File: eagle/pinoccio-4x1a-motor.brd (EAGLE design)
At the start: 25.4 x 43.2 mm, 11 parts, among them IC1 74LVC1G04DBV, J1 POWER_JACKPTH, U1 TB6621FNG, U2 TB6621FNG

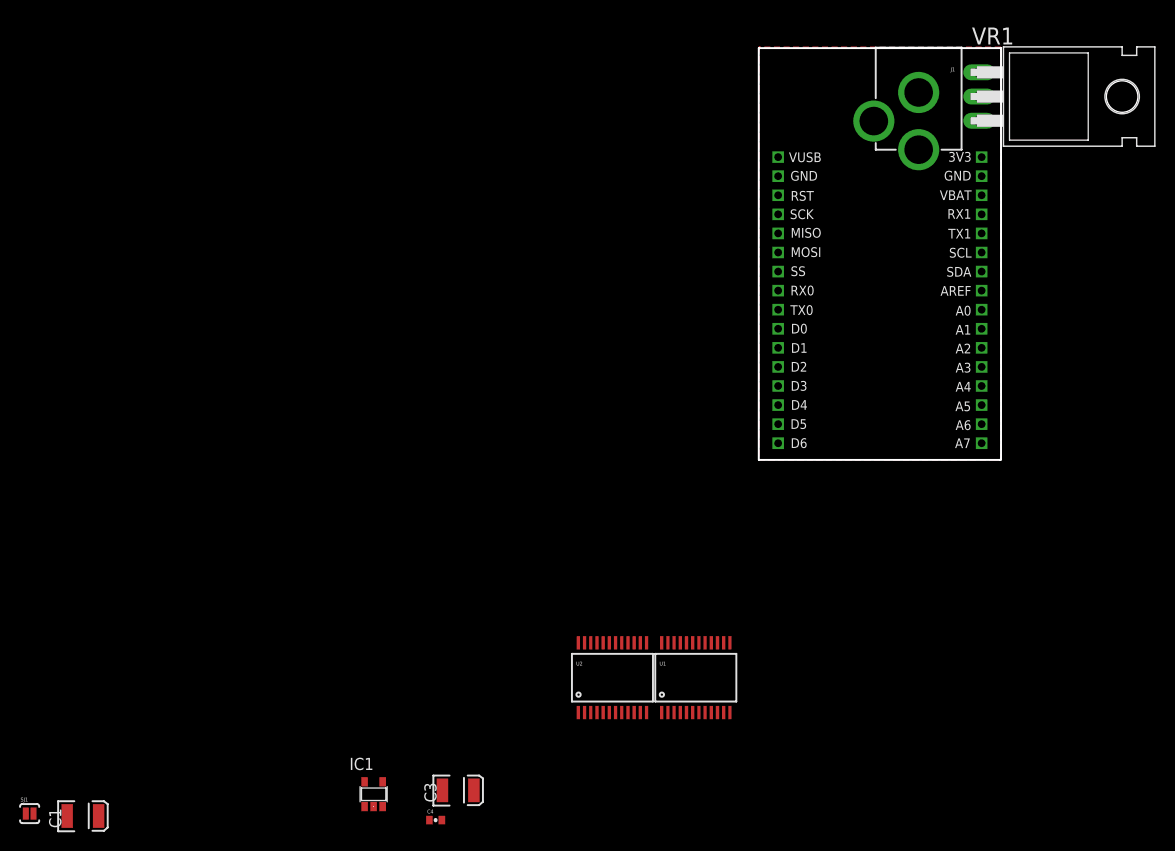
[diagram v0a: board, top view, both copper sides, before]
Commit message: Finish first draft of schematic
Initial placement.
Add design rules file from OSHPark.com
Export PDFs of schematic and board.
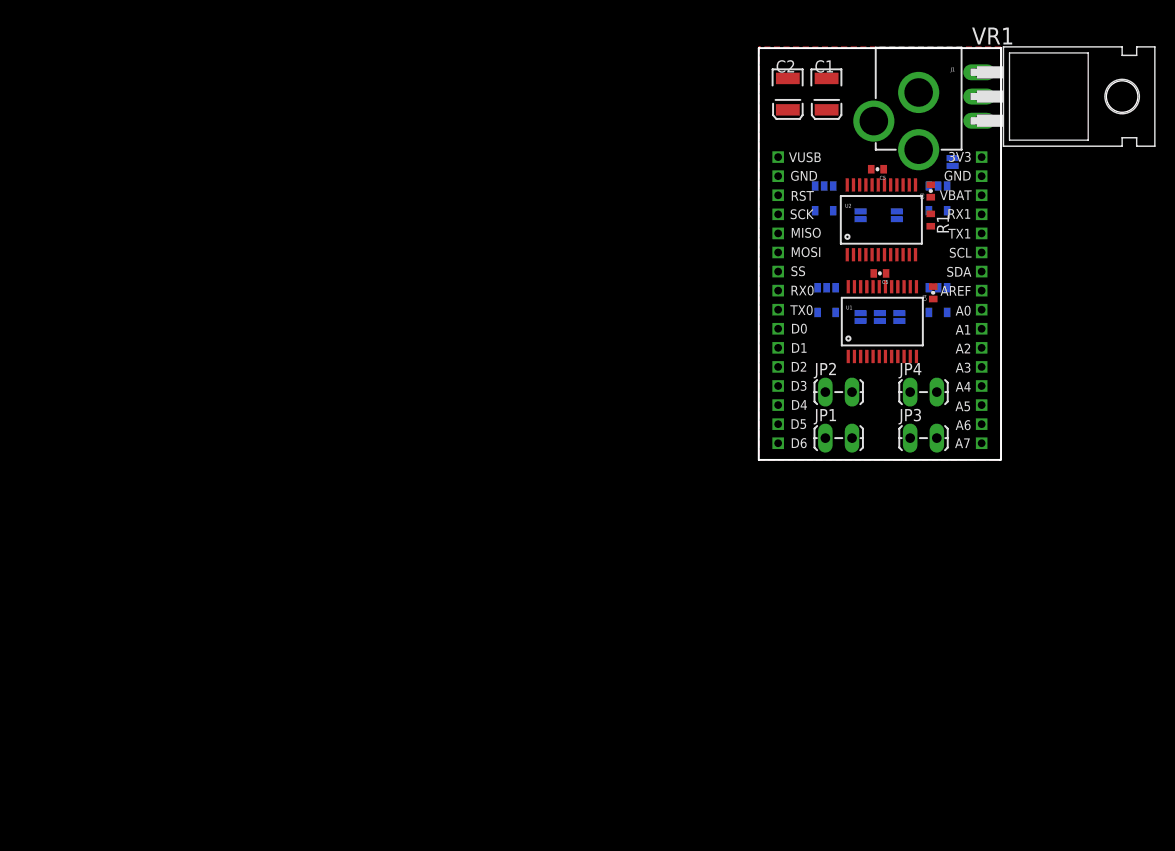
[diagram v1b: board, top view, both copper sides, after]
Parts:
- added C2: 10uf , 20V, SparkFun:EIA3528
- added C5, C6: 0.1uF, SparkFun:0402-CAP
- added IC2, IC3, IC4: 74LVC1G04DBV, 74xx-little-de:SOT23-5
- added JP1, JP2, JP3, JP4: (no value), SparkFun-Connectors:1X02_LOCK_LONGPADS
- added R1: 10k, rcl:R0402
- added SJ2, SJ3, SJ4, SJ5, SJ6: SOLDERJUMPERNC2, SparkFun-Passives:SJ_2S-NOTRACE
- C3: value 10uf , 20V -> 0.1uF; device SparkFun:EIA3528 -> SparkFun:0402-CAP
- moved C1 108.7 mm to (7.11, 46.0), turned to 270 degrees
- moved SJ1 101.5 mm to (10.7, 22.6), flipped to the bottom, turned to 270 degrees
- moved C3 80.0 mm to (18.0, 35.8), turned to 90 degrees
- moved C4 76.0 mm to (18.3, 25.1), turned to 90 degrees
- moved IC1 70.3 mm to (7.11, 24.4), flipped to the bottom, turned to 180 degrees
- moved U2 55.7 mm to (12.9, 32.8)
- moved U1 42.2 mm to (13.0, 22.1)
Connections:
- net N$3 renamed 1A2
- removed net N$1: C1.A, C3.A, C4.2, VR1.3
- removed net N$2: IC1.2, U1.21
- removed net N$4: SJ1.2
- removed net VCC: IC1.5
- new net 1B2: IC2.4, SJ2.1, U1.16
- new net 2A2: IC3.4, SJ3.1, U2.22
- new net 2B2: IC4.4, SJ4.1, U2.16
- new net M1+: JP1.2, U1.1, U1.2
- new net M1-: JP1.1, U1.5, U1.6
- new net M2+: JP2.2, U1.7, U1.8
- new net M2-: JP2.1, U1.11, U1.12
- new net M3+: JP3.2, U2.1, U2.2
- new net M3-: JP3.1, U2.5, U2.6
- new net M4+: JP4.2, U2.7, U2.8
- new net N$8: JP4.1, U2.11, U2.12
- new net STBY: R1.2, SJ5.1, U1.19, U2.19
- new net V+: C1.A, C2.A, C3.2, C4.2, J1.PWR, SJ6.1, U1.13, U1.14, U1.24, U2.13, U2.14, U2.24, VR1.3
- net A2: now also SJ4.2
- net A3: now also SJ3.2
- net A4: now also SJ2.2
- net A5: now also SJ1.2
- net A6: now also IC4.2, U2.17
- net A7: now also SJ5.2
- net D0: now also U1.23
- net D1: now also U1.15
- net D2: now also U2.23
- net D3: now also U2.15
- net D4: now also IC1.2, U1.21
- net D5: now also IC2.2, U1.17
- net D6: now also IC3.2, U2.21
- net GND: now also C2.C, C3.1, C5.1, C6.1, IC2.3, IC3.3, IC4.3, J1.GND, J1.GNDBREAK, U1.10, U1.18, U1.3, U1.4, U1.9, U2.10, U2.18, U2.3, U2.4, U2.9; no longer C3.C
- net VBAT-AE: now also SJ6.2
- net VCC-AE: now also C5.2, C6.2, IC1.5, IC2.5, IC3.5, IC4.5, R1.1, U1.20, U2.20
- net VUSB: now also VR1.2
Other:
- board text added: "Design by: Daniel Casner referencing design by Eric Jennings for Pinoccio"
- board text added: "http://danielcasner.org http://pinocc.io"
- board text removed: "Design by: Eric Jennings for Pinoccio"
- board text removed: "http://pinocc.io"

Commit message: Working on manual routing.
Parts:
- moved JP3 16.4 mm to (10.7, 25.4), turned to 180 degrees
- moved JP2 11.0 mm to (17.0, 9.91), turned to 180 degrees
- moved JP4 10.7 mm to (17.0, 25.4), turned to 180 degrees
- moved U1 5.37 mm to (12.7, 16.8)
- moved SJ1 5.34 mm to (10.4, 17.3)
- moved SJ2 5.34 mm to (14.5, 17.3)
- moved SJ5 5.34 mm to (12.4, 17.3)
- moved C4 5.34 mm to (18.0, 19.8)
- moved C6 5.34 mm to (12.4, 21.8)
- moved IC1 5.34 mm to (6.86, 19.1)
- moved IC2 5.34 mm to (18.5, 19.1)
- moved JP1 3.81 mm to (10.9, 9.91), turned to 180 degrees
- moved SJ6 3.81 mm to (23.4, 41.1), turned to 180 degrees
- moved C5 0.36 mm to (12.2, 37.8)
- moved IC3 0.36 mm to (6.60, 34.8)
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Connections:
- net N$8 renamed M4-
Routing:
- net V+: track 0.00 -> 79.8 mm
- net VUSB: track 0.00 -> 37.4 mm
- net VBAT-AE: track 0.00 -> 8.03 mm
- net VCC-AE: track 0.00 -> 3.21 mm
- added copper zone on layer 1, net M1+
- added copper zone on layer 1, net M1-
- added copper zone on layer 1, net M2+
- added copper zone on layer 1, net M2-
- added copper zone on layer 1, net M3+
- added copper zone on layer 1, net M3-
- added copper zone on layer 1, net M4+
- added copper zone on layer 1, net M4-

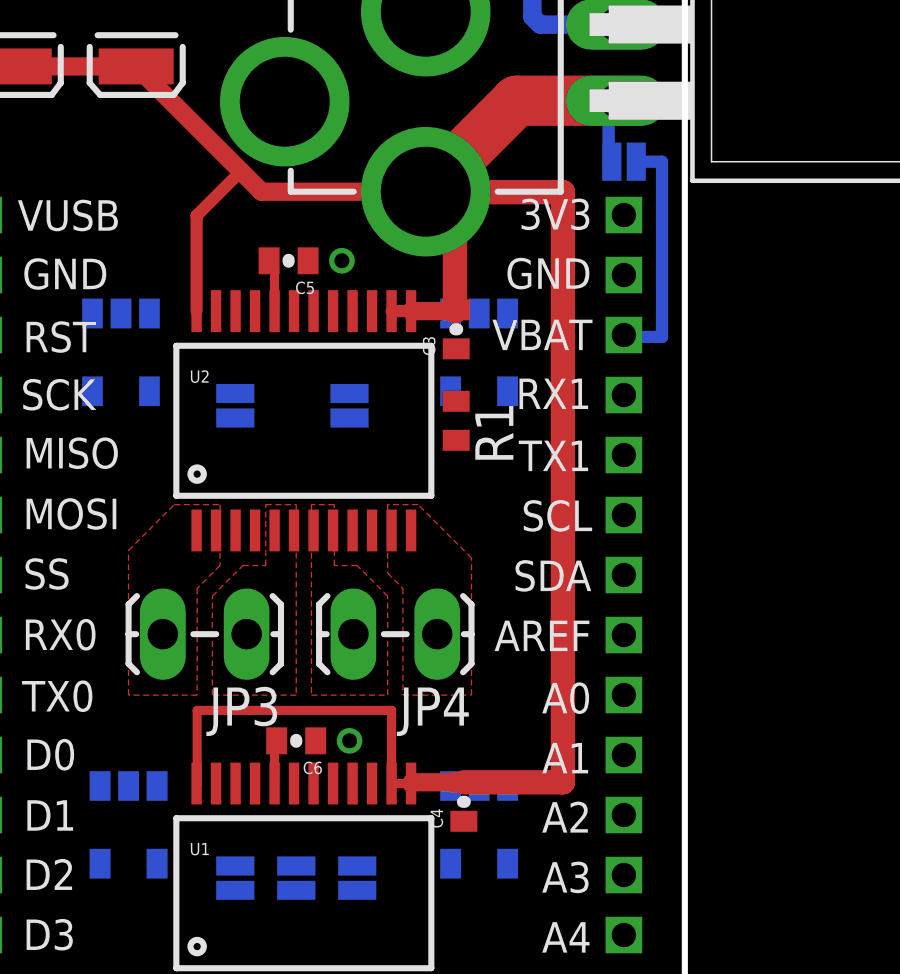
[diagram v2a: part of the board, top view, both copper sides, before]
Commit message: A tiny bit more work. Putting everything on hold until the new backpack interface is documented.
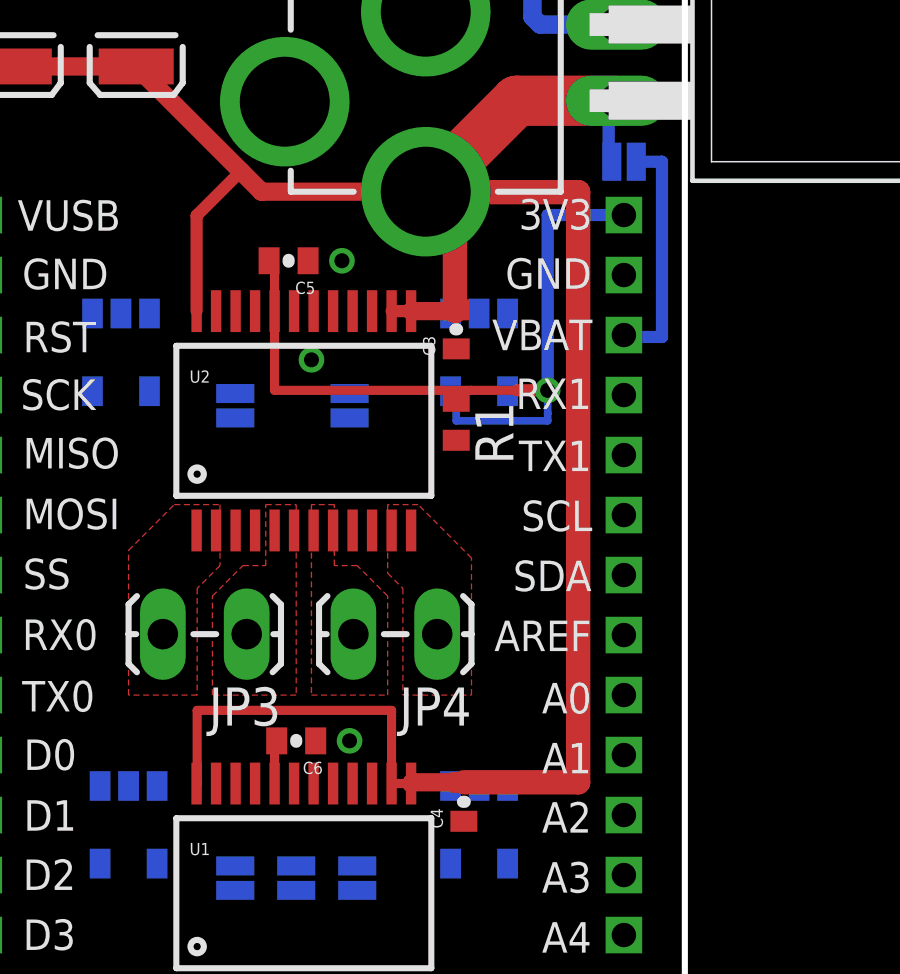
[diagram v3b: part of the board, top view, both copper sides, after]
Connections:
- new net BKPK-BUS: JP-L.P$2
- net GND: no longer JP-L.P$2
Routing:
- net VCC-AE: track 3.21 -> 29.9 mm, vias 0 -> 1
- net V+: track 79.8 -> 80.9 mm
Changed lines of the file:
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@@
 <signals>
 <signal name="GND" class="5">
-<contactref element="JP-L" pad="P$2"/>
 <contactref element="JP-R" pad="P$2"/>
 <polygon width="0.4064" layer="1" rank="6">
@@
 <via x="13.97" y="37.846" extent="1-16" drill="0.5"/>
 <via x="14.224" y="21.844" extent="1-16" drill="0.5"/>
+<via x="12.954" y="34.544" extent="1-16" drill="0.5"/>
 </signal>
 <signal name="MOSI">
@@
 <wire x1="11.725" y1="20.42" x2="11.725" y2="21.773" width="0.3048" layer="1"/>
 <wire x1="11.725" y1="21.773" x2="11.796" y2="21.844" width="0.3048" layer="1"/>
-<wire x1="17.592" y1="33.498" x2="23.368" y2="39.37" width="0" layer="19" extent="16-16"/>
-<wire x1="17.78" y1="33.162" x2="17.592" y2="33.498" width="0" layer="19" extent="1-16"/>
-<wire x1="11.725" y1="36.168" x2="17.592" y2="33.498" width="0" layer="19" extent="1-16"/>
-<wire x1="5.654" y1="33.498" x2="11.725" y2="36.168" width="0" layer="19" extent="1-16"/>
-<wire x1="11.796" y1="21.844" x2="17.78" y2="33.162" width="0" layer="19" extent="1-1"/>
+<wire x1="23.368" y1="39.37" x2="20.828" y2="39.37" width="0.4064" layer="16"/>
+<wire x1="20.828" y1="39.37" x2="20.828" y2="33.528" width="0.4064" layer="16"/>
+<via x="20.828" y="33.528" extent="1-16" drill="0.5"/>
+<wire x1="20.828" y1="33.528" x2="19.812" y2="33.528" width="0.4064" layer="1"/>
+<wire x1="19.812" y1="33.528" x2="18.288" y2="33.528" width="0.3048" layer="1"/>
+<wire x1="18.288" y1="33.528" x2="11.725" y2="33.528" width="0.3048" layer="1"/>
+<wire x1="11.725" y1="33.528" x2="11.725" y2="36.168" width="0.3048" layer="1"/>
+<wire x1="17.592" y1="33.498" x2="17.526" y2="33.498" width="0.254" layer="16"/>
+<wire x1="20.828" y1="32.766" x2="20.828" y2="33.528" width="0.254" layer="16"/>
+<wire x1="17.592" y1="33.498" x2="17.78" y2="33.498" width="0.254" layer="16"/>
+<wire x1="17.78" y1="33.498" x2="17.78" y2="32.512" width="0.254" layer="16"/>
+<wire x1="17.78" y1="32.512" x2="20.828" y2="32.512" width="0.254" layer="16"/>
+<wire x1="20.828" y1="32.512" x2="20.828" y2="32.766" width="0.254" layer="16"/>
+<wire x1="17.78" y1="33.162" x2="17.592" y2="33.162" width="0.254" layer="1"/>
+<wire x1="17.592" y1="33.162" x2="17.592" y2="33.498" width="0.254" layer="1"/>
+<wire x1="17.592" y1="33.498" x2="18.288" y2="33.498" width="0.254" layer="1"/>
+<wire x1="18.288" y1="33.498" x2="18.288" y2="33.528" width="0.254" layer="1"/>
+<wire x1="5.654" y1="33.498" x2="11.725" y2="33.528" width="0" layer="19" extent="1-16"/>
+<wire x1="11.796" y1="21.844" x2="11.725" y2="33.528" width="0" layer="19" extent="1-1"/>
 <wire x1="5.908" y1="17.75" x2="11.725" y2="20.42" width="0" layer="19" extent="1-16"/>
 <wire x1="17.592" y1="17.75" x2="11.725" y2="20.42" width="0" layer="19" extent="1-16"/>
@@
 <wire x1="17.738" y1="36.168" x2="17.78" y2="36.21" width="0.4064" layer="1"/>
 <wire x1="16.275" y1="39.659" x2="16.764" y2="40.148" width="0.4064" layer="1"/>
-<wire x1="18.034" y1="20.462" x2="21.336" y2="20.462" width="0.8128" layer="1"/>
-<wire x1="21.336" y1="20.462" x2="21.336" y2="40.132" width="0.8128" layer="1"/>
-<wire x1="21.336" y1="40.132" x2="16.256" y2="40.132" width="0.8128" layer="1"/>
+<wire x1="18.034" y1="20.462" x2="21.844" y2="20.462" width="0.8128" layer="1"/>
+<wire x1="21.844" y1="20.462" x2="21.844" y2="40.132" width="0.8128" layer="1"/>
+<wire x1="21.844" y1="40.132" x2="16.256" y2="40.132" width="0.8128" layer="1"/>
 <wire x1="16.256" y1="40.132" x2="16.256" y2="40.148" width="0.8128" layer="1"/>
 <wire x1="17.738" y1="36.168" x2="17.738" y2="39.174" width="0.8128" layer="1"/>
@@
 <contactref element="U2" pad="12"/>
 </signal>
+<signal name="BKPK-BUS" class="5">
+<contactref element="JP-L" pad="P$2"/>
+</signal>
 </signals>

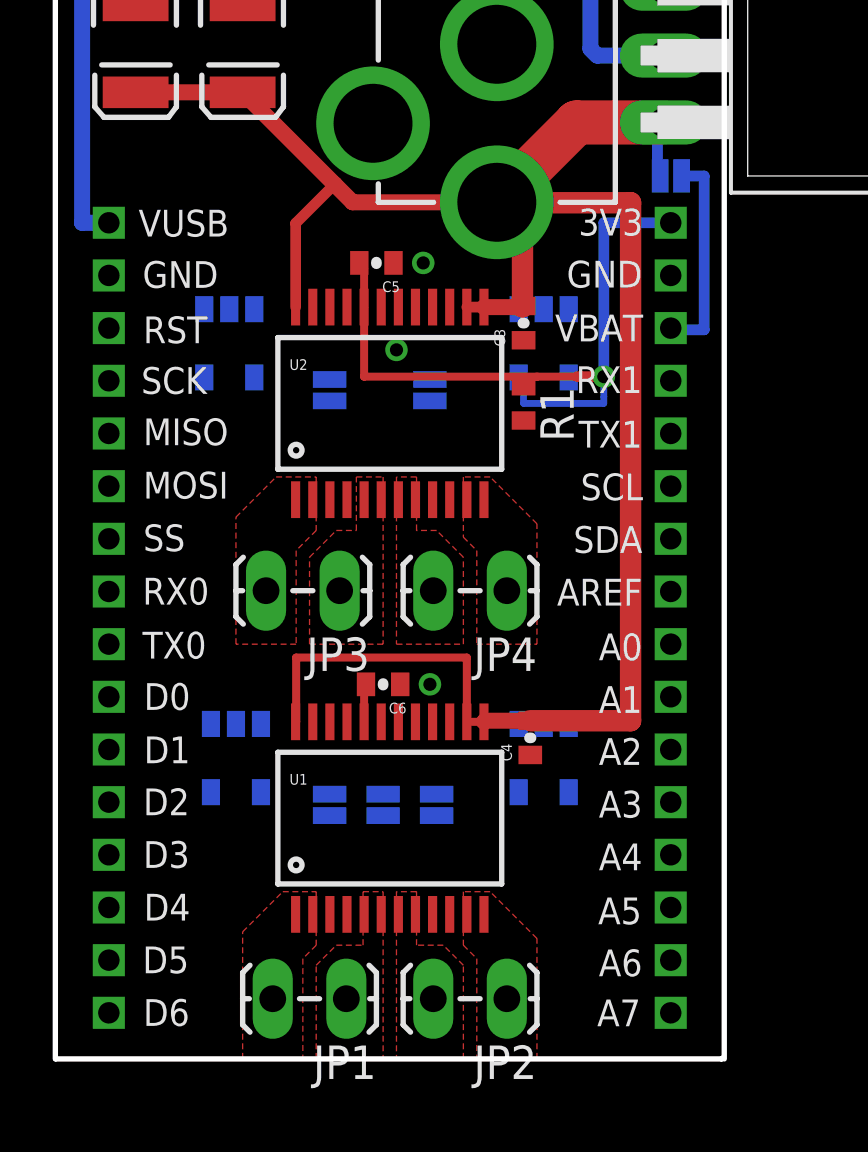
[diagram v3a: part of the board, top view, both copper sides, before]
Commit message: Finish routing with auto-router. Export PDFs of schematic and board.
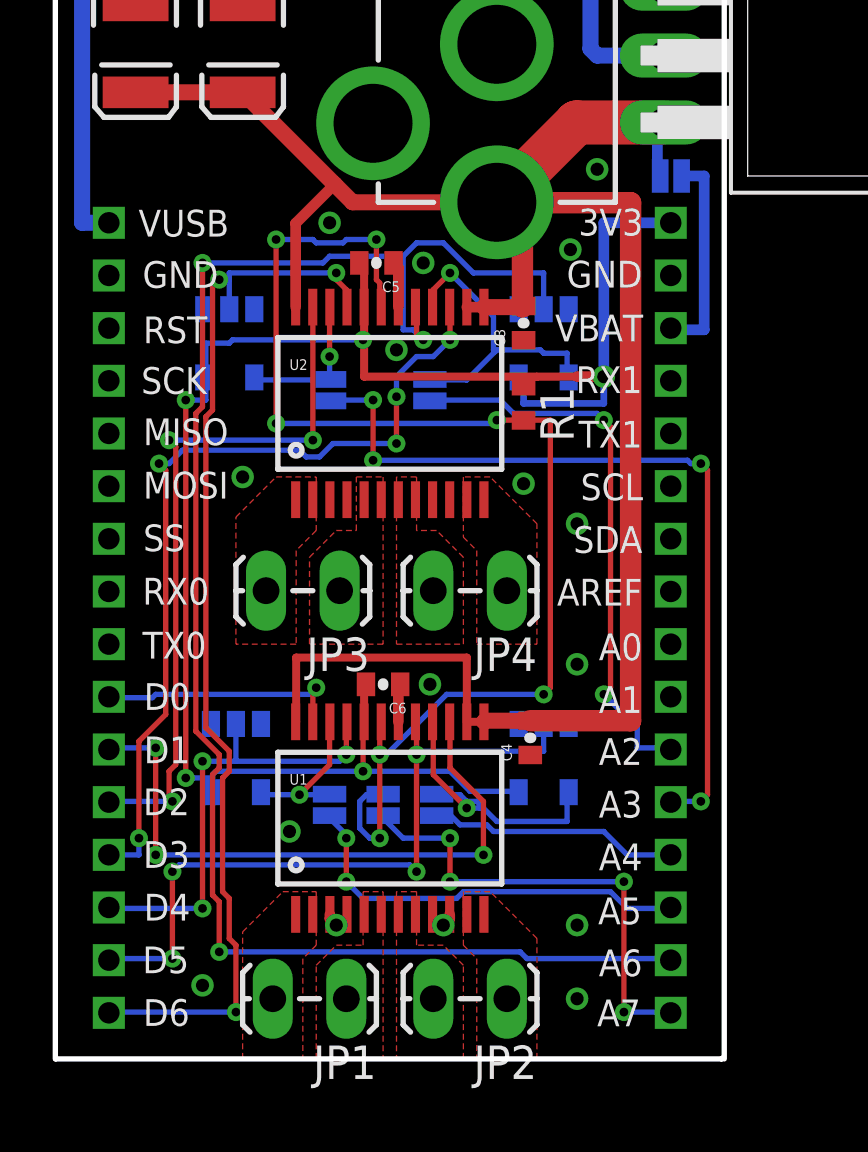
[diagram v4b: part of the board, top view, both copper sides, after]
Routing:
- net A6: track 0.00 -> 64.3 mm, vias 0 -> 3
- net STBY: track 0.00 -> 49.1 mm, vias 0 -> 7
- net D6: track 0.00 -> 40.8 mm, vias 0 -> 3
- net VCC-AE: track 29.9 -> 68.9 mm, vias 1 -> 5
- net D3: track 0.00 -> 32.5 mm, vias 0 -> 5
- net A3: track 0.00 -> 30.7 mm, vias 0 -> 4
- net D2: track 0.00 -> 26.9 mm, vias 0 -> 3
- net D5: track 0.00 -> 26.9 mm, vias 0 -> 4
- net D1: track 0.00 -> 23.9 mm, vias 0 -> 3
- net A2: track 0.00 -> 21.5 mm, vias 0 -> 2
- net A7: track 0.00 -> 18.0 mm, vias 0 -> 4
- net D4: track 0.00 -> 17.4 mm, vias 0 -> 3
- net A5: track 0.00 -> 15.8 mm, vias 0 -> 2
- net 2B2: track 0.00 -> 12.0 mm, vias 0 -> 1
- net 1B2: track 0.00 -> 10.9 mm, vias 0 -> 1
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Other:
- board text added: "4x 1A motor driver backpack for Pinoccio"
- board text removed: "Pinoccio(tm) Proto v0.9"
